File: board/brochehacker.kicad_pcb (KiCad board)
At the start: 2 copper layers, 38.7 x 41.9 mm, 8 parts, among them IC1 ATMEGA328-P, P1 CONN_01X02, Y1 16MHz

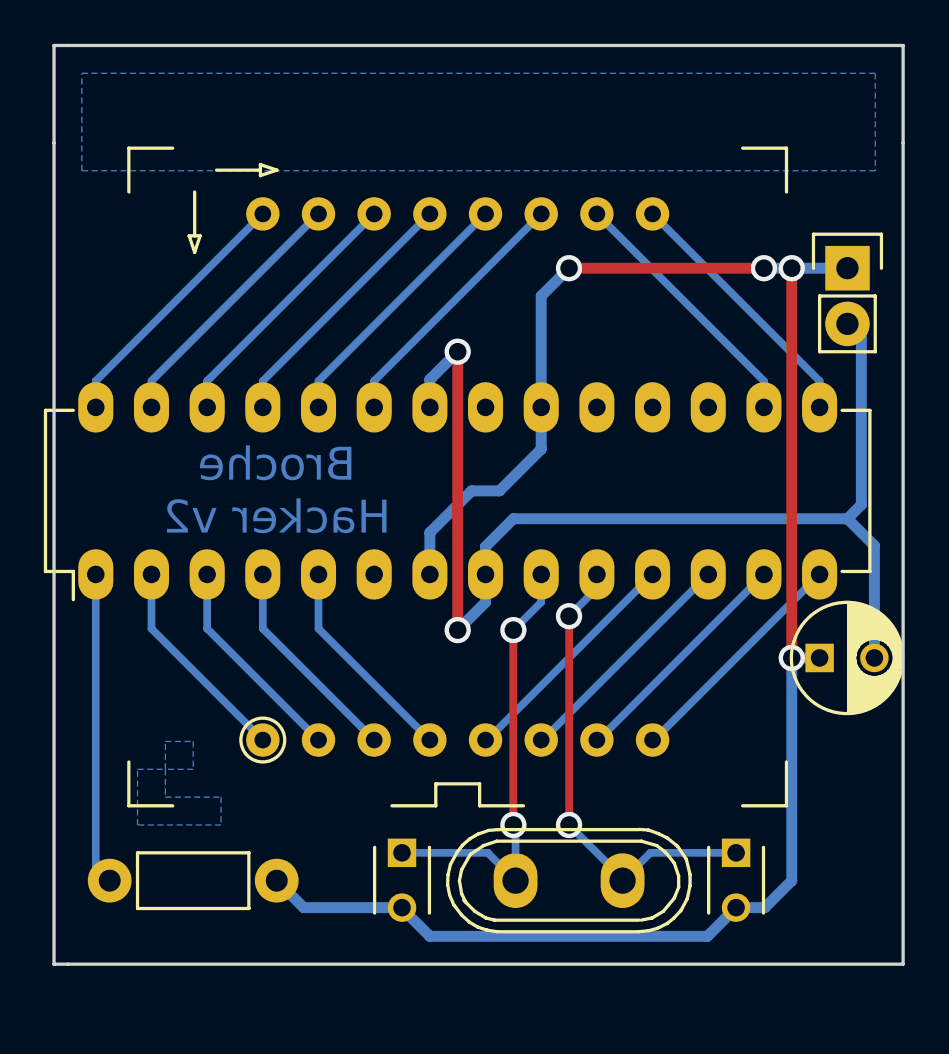
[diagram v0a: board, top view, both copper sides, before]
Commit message: conserta cristal e reajusta jumpers
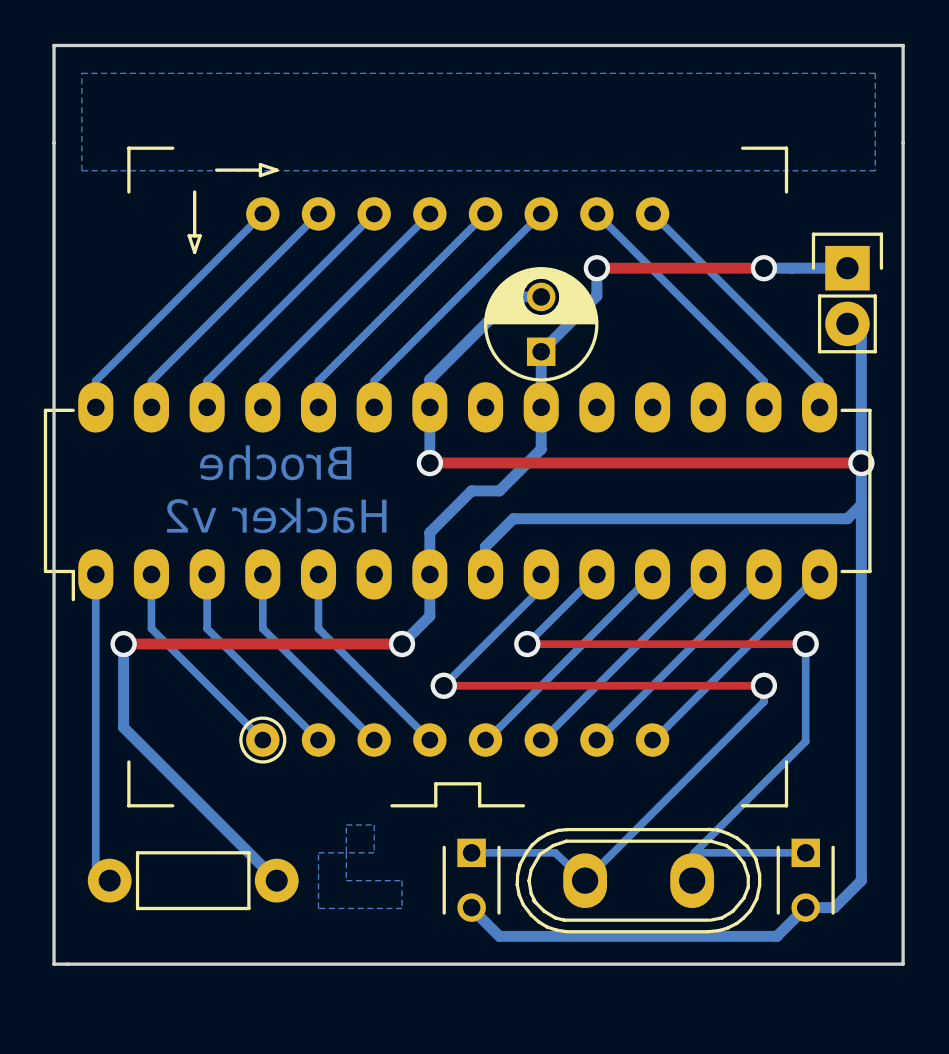
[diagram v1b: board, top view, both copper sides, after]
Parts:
- moved C2 18.9 mm to (166.4, 111.8), turned to 90 degrees
- moved C1 3.18 mm to (178.4, 134.6)
- moved Y1 3.18 mm to (170.8, 135.9)
- moved C3 3.17 mm to (163.2, 134.6)
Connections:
- C1 pad 2: VCC -> GND
- C3 pad 2: VCC -> GND
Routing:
- net GND: track 53.4 -> 94.4 mm
- net VCC: track 84.9 -> 60.0 mm
- net Net-(C3-Pad1): track 20.2 -> 39.5 mm
- net Net-(C1-Pad1): track 21.3 -> 36.1 mm

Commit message: remove cristal, adiciona botões
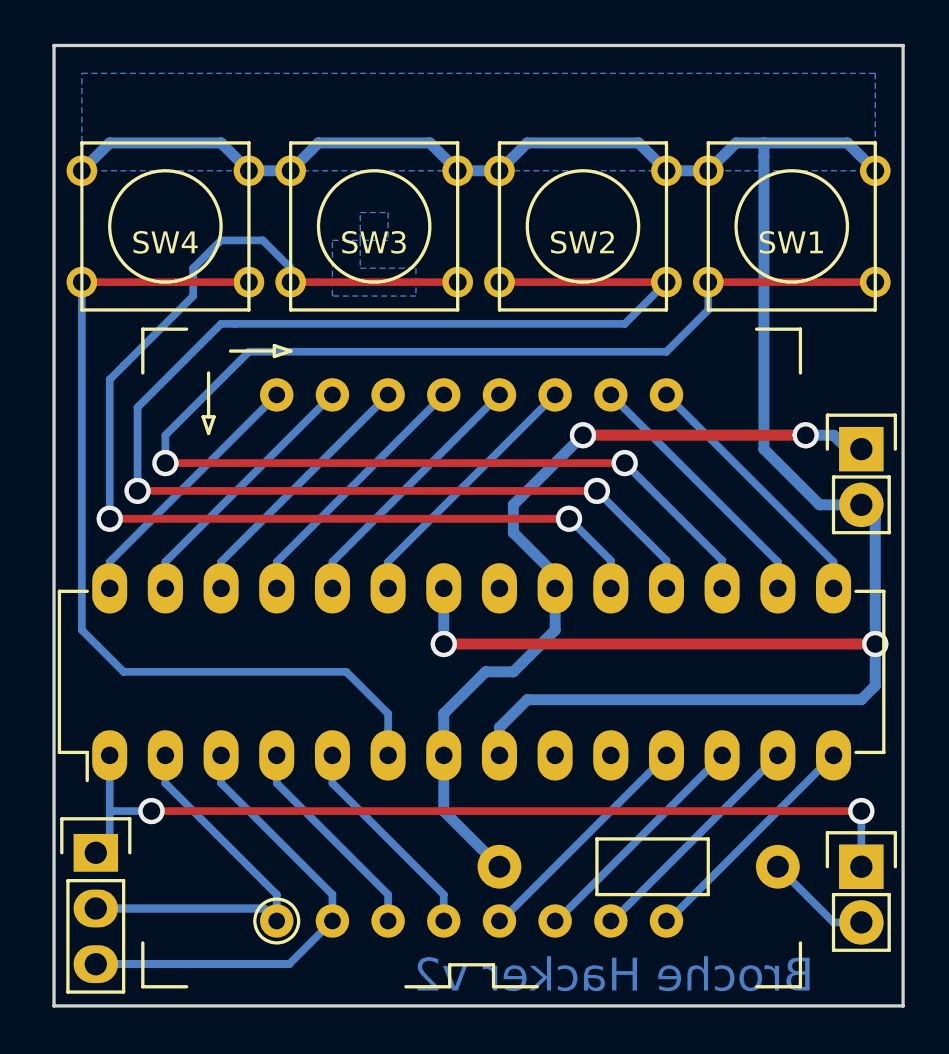
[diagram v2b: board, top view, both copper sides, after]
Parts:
- removed C1, C3: 22pF, Capacitors_ThroughHole:C_Disc_D3_P2.5
- removed C2: 100uF, Capacitors_ThroughHole:C_Radial_D5_L6_P2.5
- removed Y1: 16MHz, Crystals:Crystal_HC50-U_Vertical
- added JP1: JUMPER, Pin_Headers:Pin_Header_Straight_1x02, F.Cu at (181.0, 135.3)
- added P2: CONN_01X03, Pin_Headers:Pin_Header_Straight_1x03, F.Cu at (146.1, 134.6)
- added SW1: SW_PUSH, Buttons_Switches_ThroughHole:SW_PUSH_SMALL, F.Cu at (177.8, 106.0)
- added SW2: SW_PUSH, Buttons_Switches_ThroughHole:SW_PUSH_SMALL, F.Cu at (168.3, 106.0)
- added SW3: SW_PUSH, Buttons_Switches_ThroughHole:SW_PUSH_SMALL, F.Cu at (158.8, 106.0)
- added SW4: SW_PUSH, Buttons_Switches_ThroughHole:SW_PUSH_SMALL, F.Cu at (149.2, 106.0)
- moved R1 13.4 mm to (167.6, 135.3), turned to 0 degrees
- moved D1 8.28 mm to (163.2, 125.7)
- moved IC1 8.28 mm to (146.7, 130.2)
- moved P1 8.28 mm to (181.0, 116.2)
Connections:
- R1 pad 2: Net-(IC1-Pad1) -> Net-(JP1-Pad2)
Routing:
- net Net-(IC1-Pad17): track 0.00 -> 66.4 mm, vias 0 -> 2
- net Net-(IC1-Pad18): track 0.00 -> 65.3 mm, vias 0 -> 2
- net Net-(IC1-Pad19): track 0.00 -> 52.3 mm, vias 0 -> 2
- net Net-(IC1-Pad6): track 0.00 -> 40.9 mm
- net Net-(IC1-Pad9): track 39.5 -> 0.63 mm, vias 2 -> 0
- net Net-(IC1-Pad10): track 36.1 -> 0.63 mm, vias 2 -> 0
- net Net-(IC1-Pad1): track 14.2 -> 41.5 mm, vias 0 -> 2
- net VCC: track 60.0 -> 38.7 mm, vias 4 -> 2
- net /ROW7: track 9.66 -> 29.5 mm
- net /ROW5: track 9.66 -> 25.2 mm
- net GND: track 94.4 -> 109.8 mm
- net Net-(JP1-Pad2): track 0.00 -> 4.86 mm
- added copper zone on B.Cu, net GND
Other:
- board size 38.7 x 41.9 mm -> 38.7 x 43.8 mm
- board text added: "P"

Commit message: novos pads de alfinete
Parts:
- added REF**: safety_pin_2.5_3.5_4.5mm, safety_pin:safety_pin_2.5_3.5_4.5mm, B.Cu at (164.1, 105.9)
- moved SW3 19.1 mm to (177.8, 106.0)
- moved SW1 9.53 mm to (168.3, 106.0)
- moved SW2 9.53 mm to (158.8, 106.0)
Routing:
- net Net-(IC1-Pad19): track 52.3 -> 71.3 mm, vias 2 -> 4
- net Net-(IC1-Pad17): track 66.4 -> 56.2 mm
- net Net-(IC1-Pad18): track 65.3 -> 55.4 mm
- net GND: track 109.8 -> 117.7 mm
- removed copper zone on B.Cu, net GND
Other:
- board size 38.7 x 43.8 mm -> 38.7 x 40 mm

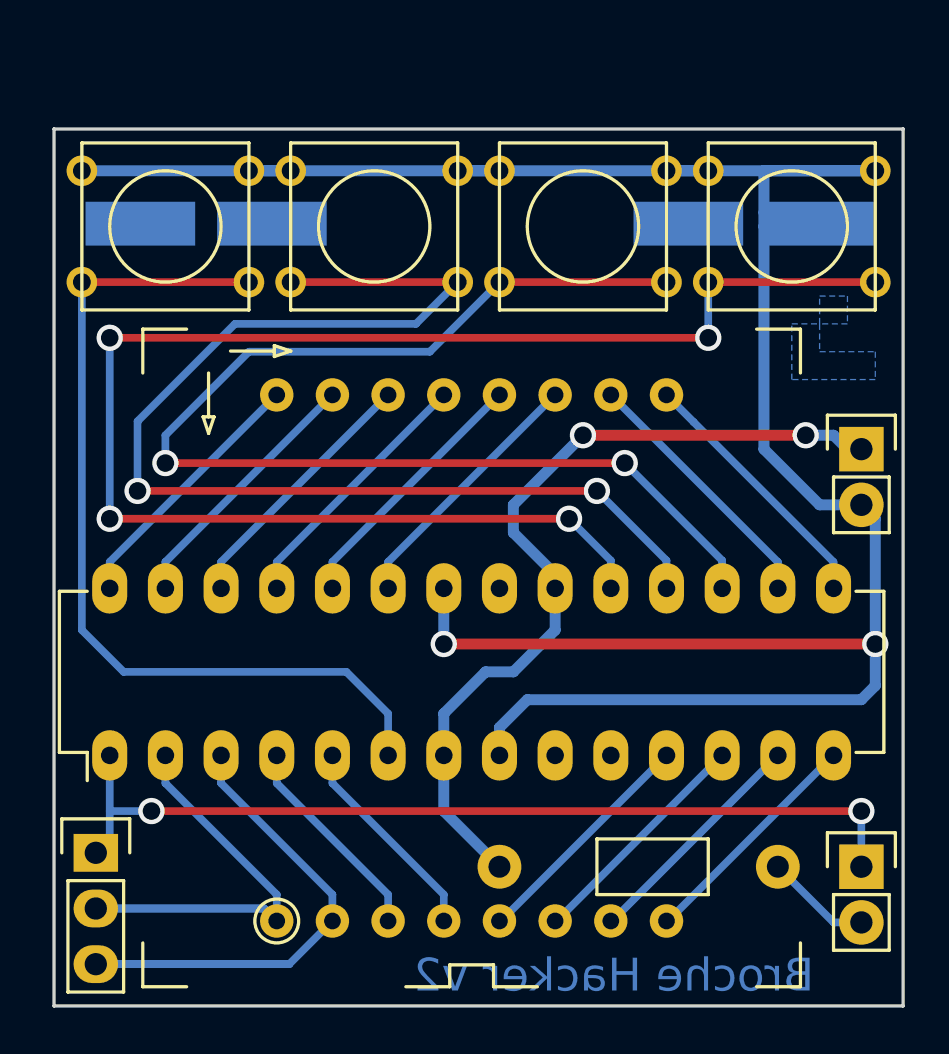
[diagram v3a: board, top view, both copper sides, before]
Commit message: remoção de jumper e traços mais grossos
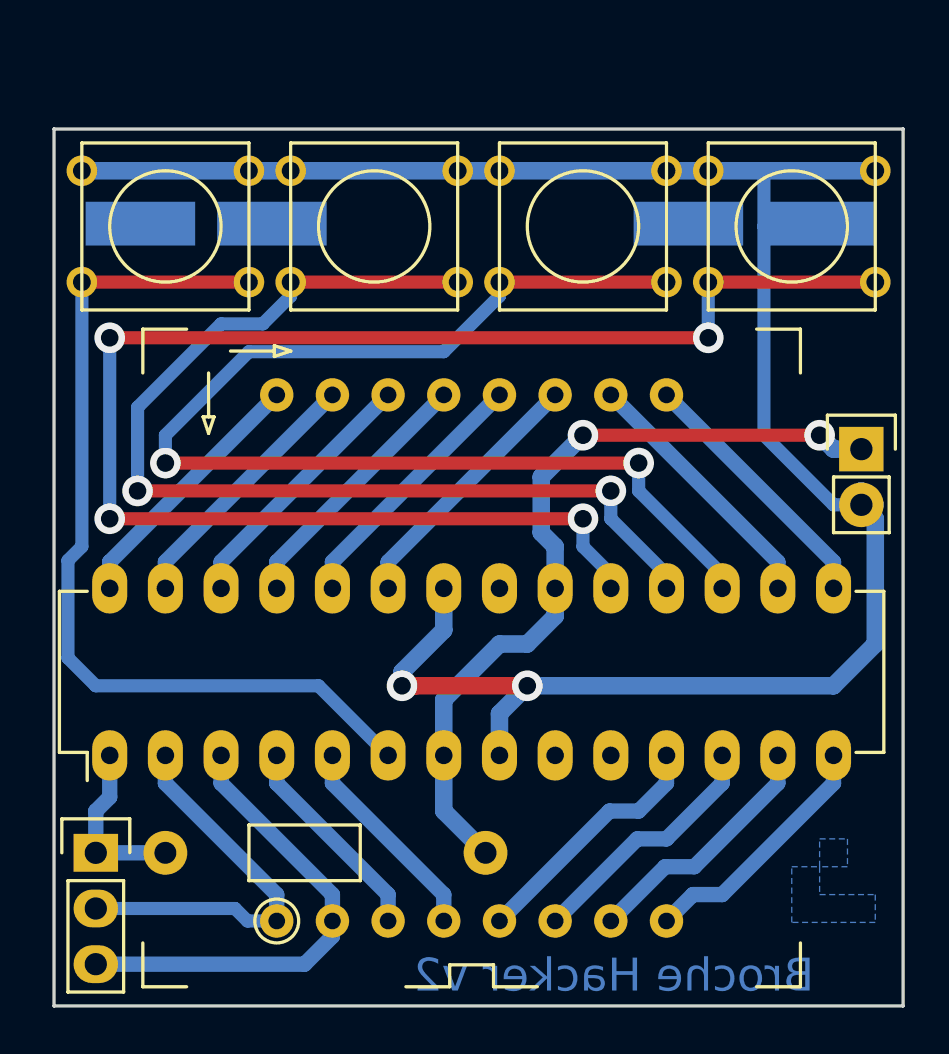
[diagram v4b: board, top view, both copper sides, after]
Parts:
- removed JP1: JUMPER, Pin_Headers:Pin_Header_Straight_1x02
- moved R1 8.28 mm to (159.4, 134.6), turned to 180 degrees
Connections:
- R1 pad 2: Net-(JP1-Pad2) -> Net-(IC1-Pad1)
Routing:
- net Net-(IC1-Pad1): track 41.5 -> 7.88 mm, vias 2 -> 0
- net GND: track 117.7 -> 96.1 mm
- net /ROW7: track 29.5 -> 21.7 mm
- net /ROW5: track 25.2 -> 18.2 mm
- net Net-(IC1-Pad18): track 55.4 -> 48.9 mm
- net Net-(JP1-Pad2): track 4.86 -> 0.00 mm
- net VCC: track 38.7 -> 36.7 mm
- net Net-(IC1-Pad17): track 56.2 -> 56.9 mm
- net /ROW8: track 10.7 -> 11.5 mm
- net /ROW3: track 10.7 -> 11.5 mm
- net /COL5: track 10.7 -> 11.5 mm
- net /ROW6: track 10.7 -> 11.5 mm
- net Net-(IC1-Pad9): track 0.63 -> 0.00 mm
- net Net-(IC1-Pad10): track 0.63 -> 0.00 mm
- net Net-(IC1-Pad6): track 40.9 -> 41.5 mm
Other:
- net class Default: trace_width 0.35 -> 0.6; via_dia 1.2 -> 1.4
- net class Power: trace_width 0.5 -> 0.8; via_dia 1.2 -> 1.4
- board text removed: "P"
